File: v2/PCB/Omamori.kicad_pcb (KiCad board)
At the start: 2 copper layers, 25 x 35 mm, 27 parts, among them J1 Conn_01x04_Female, U1 BQ25504, U2 TPS61222DCK, U3 ATtiny85

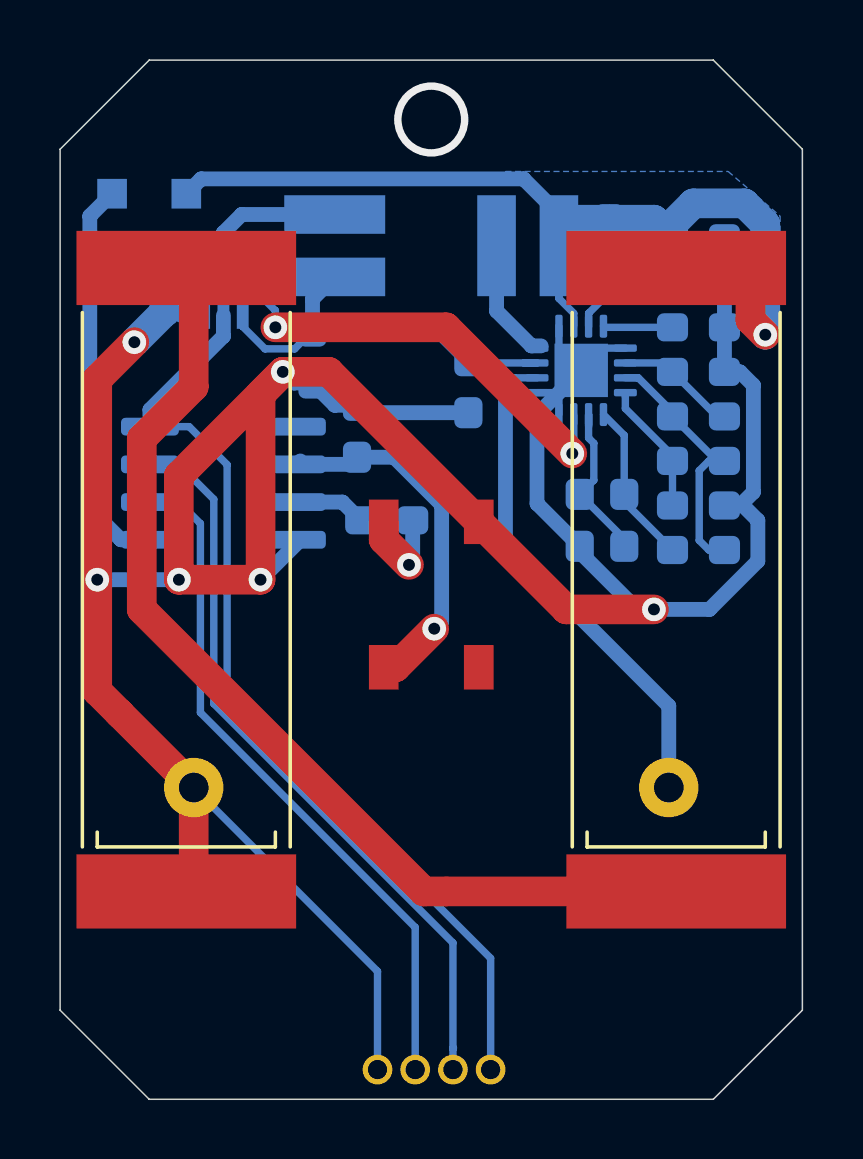
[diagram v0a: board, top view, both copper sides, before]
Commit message: Added reset button and changed a few wires.
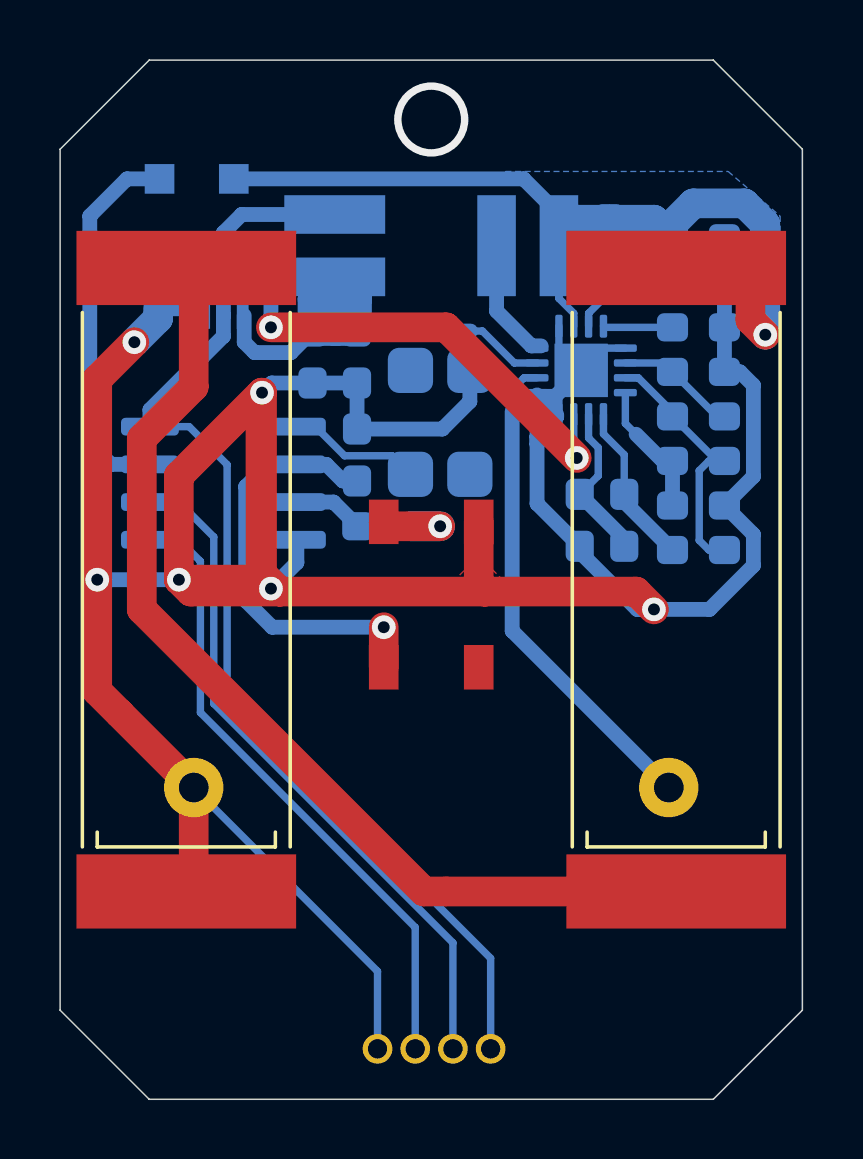
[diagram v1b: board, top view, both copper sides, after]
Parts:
- added U4: TS-1233, own_footprints:TS-1233, B.Cu at (25.3, 24.7)
- moved C_filter1 3.88 mm to (22.5, 22.5)
- moved D2 1.68 mm to (17.1, 16.5), turned to 180 degrees
- moved C_led1 0.80 mm to (22.5, 25.8)
- moved J1 0.70 mm to (27.0, 45.8)
- moved R_data1 0.22 mm to (23.4, 28.2)
- moved C_post_boost1 0.20 mm to (15.8, 20.0)
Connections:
- D1 pad 4: Net-(D1-Pad4) -> (no net)
- U3 pad 1: Net-(U3-Pad1) -> /Reset
- U3 pad 5: /Vsolar_measure -> /Tx
- U3 pad 6: /Tx -> /Rx
- U3 pad 7: /Rx -> /Vsolar_measure
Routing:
- net GND: track 115.7 -> 128.4 mm
- net /Vstor: track 14.0 -> 21.1 mm
- net /Reset: track 0.00 -> 4.49 mm
- net /Vcc_LED: track 13.1 -> 15.2 mm
- net /Rx: track 25.2 -> 23.2 mm
- net /Tx: track 23.4 -> 21.4 mm
- net /Vsolar: track 34.4 -> 32.5 mm
- net /Vcc_ATTiny: track 35.9 -> 34.9 mm
- net /Vsolar_measure: track 13.4 -> 12.8 mm

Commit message: Updated program and modified PCB Layout to measure V_supercap.
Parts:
- moved D2 15.3 mm to (15.3, 31.7), turned to 90 degrees
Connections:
- net /Vsolar_measure renamed /Vmeasure
- D2 pad 2: /Vsolar -> Net-(C_super1-Pad1)
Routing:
- net Net-(C_super1-Pad1): track 16.8 -> 31.8 mm, vias 0 -> 2
- net /Vsolar: track 32.5 -> 23.3 mm
- net /Vmeasure: track 12.8 -> 6.16 mm
- net GND: track 128.4 -> 129.8 mm
- net Net-(Sol_1-Pad2): track 33.9 -> 35.3 mm
- removed copper zone on B.Cu, net /Vsolar

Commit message: Final version + gerber export.
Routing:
- net GND: track 129.8 -> 128.7 mm
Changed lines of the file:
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@@
   )
   (setup
-    (last_trace_width 1)
+    (last_trace_width 0.25)
     (user_trace_width 0.5)
     (user_trace_width 1)
@@
     (add_net "Net-(C_ref1-Pad1)")
     (add_net "Net-(C_super1-Pad1)")
-    (add_net "Net-(D1-Pad4)")
     (add_net "Net-(L_boost1-Pad2)")
     (add_net "Net-(L_bst1-Pad2)")
@@
     (add_net "Net-(R_uv1-Pad2)")
     (add_net "Net-(Sol_1-Pad2)")
-    (add_net "Net-(U4-Pad1)")
-    (add_net "Net-(U4-Pad4)")
   )
   (module own_footprints:TS-1233 (layer B.Cu)
@@
     )
   )
+  (gr_line (start 15.5 12.5) (end 34.5 12.5) (layer Edge.Cuts) (width 0.05))
+  (gr_line (start 34.5 12.5) (end 37.5 15.5) (layer Edge.Cuts) (width 0.05))
+  (gr_line (start 12.5 15.5) (end 15.5 12.5) (layer Edge.Cuts) (width 0.05))
   (gr_line (start 12.5 44.5) (end 12.5 15.5) (layer Edge.Cuts) (width 0.05))
   (gr_line (start 15.5 47.5) (end 12.5 44.5) (layer Edge.Cuts) (width 0.05))
@@
   (gr_line (start 37.5 44.5) (end 34.5 47.5) (layer Edge.Cuts) (width 0.05))
   (gr_line (start 37.5 15.5) (end 37.5 44.5) (layer Edge.Cuts) (width 0.05))
-  (gr_line (start 34.5 12.5) (end 37.5 15.5) (layer Edge.Cuts) (width 0.05))
-  (gr_line (start 15.5 12.5) (end 34.5 12.5) (layer Edge.Cuts) (width 0.05))
-  (gr_line (start 12.5 15.5) (end 15.5 12.5) (layer Edge.Cuts) (width 0.05))
   (via (at 25 14.5) (size 2.5) (drill 2) (layers F.Cu B.Cu) (net 0))
   (via (at 16.5 30) (size 0.8) (drill 0.4) (layers F.Cu B.Cu) (net 1))
@@
   (segment (start 23.19 43.19) (end 17 37) (width 0.25) (layer B.Cu) (net 1))
   (segment (start 16.875 36.875) (end 17 37) (width 0.25) (layer B.Cu) (net 1))
-  (segment (start 32.5 31) (end 32.5 31) (width 0.25) (layer F.Cu) (net 1))
-  (via (at 32.5 31) (size 0.8) (drill 0.4) (layers F.Cu B.Cu) (net 1))
+  (via (at 31.9 30.4) (size 0.8) (drill 0.4) (layers F.Cu B.Cu) (net 1))
   (segment (start 30 29.065685) (end 30 28.875) (width 0.25) (layer B.Cu) (net 1))
-  (segment (start 31.934315 31) (end 30 29.065685) (width 0.5) (layer B.Cu) (net 1))
-  (segment (start 32.5 31) (end 31.934315 31) (width 0.5) (layer B.Cu) (net 1))
   (via (at 19.6 30.3) (size 0.8) (drill 0.4) (layers F.Cu B.Cu) (net 1))
   (segment (start 20.475 28.655) (end 20.475 28.775) (width 0.25) (layer B.Cu) (net 1))
@@
   (segment (start 19.625 23.375) (end 19.3 23.7) (width 0.5) (layer B.Cu) (net 1))
   (segment (start 21 23.375) (end 19.625 23.375) (width 0.5) (layer B.Cu) (net 1))
-  (segment (start 32.5 31) (end 31.89999 30.39999) (width 1) (layer F.Cu) (net 1))
   (segment (start 26.6 30.2) (end 26.79999 30.39999) (width 1) (layer F.Cu) (net 1))
   (segment (start 26.6 28.05) (end 26.6 30.2) (width 1) (layer F.Cu) (net 1))
@@
   (segment (start 29 24) (end 30.05 22.95) (width 0.5) (layer B.Cu) (net 1))
   (segment (start 28.5625 27.4375) (end 30 28.875) (width 0.5) (layer B.Cu) (net 1))
-  (segment (start 35.85001 28.47501) (end 34.875 27.5) (width 0.5) (layer B.Cu) (net 1))
-  (segment (start 35.85001 29.522278) (end 35.85001 28.47501) (width 0.5) (layer B.Cu) (net 1))
-  (segment (start 34.372288 31) (end 35.85001 29.522278) (width 0.5) (layer B.Cu) (net 1))
-  (segment (start 32.5 31) (end 34.372288 31) (width 0.5) (layer B.Cu) (net 1))
   (segment (start 34.875 27.497288) (end 34.875 27.5) (width 0.5) (layer B.Cu) (net 1))
   (segment (start 35.85001 26.522278) (end 34.875 27.497288) (width 0.5) (layer B.Cu) (net 1))
@@
   (segment (start 16.1 31.7) (end 13.75 31.7) (width 0.5) (layer B.Cu) (net 1))
   (segment (start 16.5 31.3) (end 16.1 31.7) (width 0.5) (layer B.Cu) (net 1))
+  (segment (start 35.85001 29.84999) (end 35.3 30.4) (width 0.5) (layer B.Cu) (net 1))
+  (segment (start 35.3 30.4) (end 31.9 30.4) (width 0.5) (layer B.Cu) (net 1))
+  (segment (start 35.85001 28.47501) (end 35.85001 29.84999) (width 0.5) (layer B.Cu) (net 1))
+  (segment (start 34.875 27.5) (end 35.85001 28.47501) (width 0.5) (layer B.Cu) (net 1))
+  (segment (start 31.525 30.4) (end 30 28.875) (width 0.5) (layer B.Cu) (net 1))
+  (segment (start 31.9 30.4) (end 31.525 30.4) (width 0.5) (layer B.Cu) (net 1))
   (segment (start 30.8375 21.5) (end 30.8 21.4625) (width 0.25) (layer B.Cu) (net 2))
   (segment (start 33.125 21.5) (end 30.8375 21.5) (width 0.25) (layer B.Cu) (net 2))
   (segment (start 18 18.314998) (end 18 18.9) (width 0.5) (layer B.Cu) (net 3))
-  (segment (start 18.614998 17.7) (end 18 18.314998) (width 0.5) (layer B.Cu) (net 3))
-  (segment (start 18.614998 17.7) (end 21.75 17.7) (width 0.5) (layer B.Cu) (net 3))
+  (segment (start 18 18.089998) (end 18 18.314998) (width 0.5) (layer B.Cu) (net 3))
+  (segment (start 18.389998 17.7) (end 18 18.089998) (width 0.5) (layer B.Cu) (net 3))
+  (segment (start 21.75 17.7) (end 18.389998 17.7) (width 0.5) (layer B.Cu) (net 3))
   (segment (start 27.2 20.95) (end 28.37499 22.12499) (width 0.5) (layer B.Cu) (net 4))
   (segment (start 27.2 18.75) (end 27.2 20.95) (width 0.5) (layer B.Cu) (net 4))
@@
   (segment (start 18.65 21.1) (end 18.65 20.975) (width 0.25) (layer B.Cu) (net 11))
   (segment (start 22.5 21.625) (end 26.325 21.625) (width 0.5) (layer B.Cu) (net 11))
-  (segment (start 26.723452 21.625) (end 26.325 21.625) (width 0.25) (layer B.Cu) (net 11))
-  (segment (start 27.798452 22.7) (end 26.723452 21.625) (width 0.25) (layer B.Cu) (net 11))
-  (segment (start 28.5625 22.7) (end 27.798452 22.7) (width 0.25) (layer B.Cu) (net 11))
   (segment (start 19.050001 22.350001) (end 18.70001 22.00001) (width 0.5) (layer B.Cu) (net 11))
   (segment (start 18.70001 22.00001) (end 18.70001 21.1) (width 0.5) (layer B.Cu) (net 11))
@@
   (segment (start 22.5 20.55) (end 21.75 19.8) (width 1) (layer B.Cu) (net 11))
   (segment (start 22.5 21.625) (end 22.5 20.55) (width 1) (layer B.Cu) (net 11))
+  (segment (start 27.9 22.7) (end 28.5625 22.7) (width 0.25) (layer B.Cu) (net 11))
+  (segment (start 26.825 21.625) (end 27.9 22.7) (width 0.25) (layer B.Cu) (net 11))
+  (segment (start 26.325 21.625) (end 26.825 21.625) (width 0.25) (layer B.Cu) (net 11))
   (via (at 36.25 21.75) (size 0.8) (drill 0.4) (layers F.Cu B.Cu) (net 12))
   (segment (start 29.3 20.526978) (end 29.3 18.75) (width 0.25) (layer B.Cu) (net 12))
@@
   (segment (start 17.29999 19.35) (end 17.07499 19.125) (width 0.5) (layer B.Cu) (net 13))
   (segment (start 17.29999 19.659992) (end 17.29999 19.35) (width 0.5) (layer B.Cu) (net 13))
+  (segment (start 17.07499 19.125) (end 17.29999 18.9) (width 0.5) (layer B.Cu) (net 13))
   (segment (start 33.125 36.875) (end 33 37) (width 0.25) (layer B.Cu) (net 14))
   (segment (start 28.126978 23.2) (end 28.5625 23.2) (width 0.25) (layer B.Cu) (net 14))
@@
   (segment (start 25.3 28.2) (end 23.55 28.2) (width 1) (layer F.Cu) (net 18))
   (segment (start 24.275 28.2) (end 25.3 28.2) (width 1) (layer B.Cu) (net 18))
-  (segment (start 14.55 26.115) (end 13.9 26.765) (width 0.5) (layer B.Cu) (net 23))
-  (segment (start 15.525 26.115) (end 14.55 26.115) (width 0.5) (layer B.Cu) (net 23))
-  (segment (start 13.9 29.05) (end 15.3 30.45) (width 0.5) (layer B.Cu) (net 23))
-  (segment (start 13.9 26.765) (end 13.9 29.05) (width 0.5) (layer B.Cu) (net 23))
   (segment (start 25.73 45.792894) (end 25.75 45.772894) (width 0.25) (layer B.Cu) (net 19))
   (segment (start 25.73 42.23) (end 17.675011 34.175011) (width 0.25) (layer B.Cu) (net 19))
@@
   (segment (start 23.67499 25.82499) (end 22.07948 25.82499) (width 0.25) (layer B.Cu) (net 22))
   (segment (start 24.3 26.45) (end 23.67499 25.82499) (width 0.25) (layer B.Cu) (net 22))
+  (segment (start 14.55 26.115) (end 13.9 26.765) (width 0.5) (layer B.Cu) (net 23))
+  (segment (start 15.525 26.115) (end 14.55 26.115) (width 0.5) (layer B.Cu) (net 23))
+  (segment (start 13.9 29.05) (end 15.3 30.45) (width 0.5) (layer B.Cu) (net 23))
+  (segment (start 13.9 26.765) (end 13.9 29.05) (width 0.5) (layer B.Cu) (net 23))
   (zone (net 1) (net_name GND) (layer F.Cu) (hatch edge 0.508)
     (connect_pads yes (clearance 0))

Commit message: Beyond last second changes to the PCB design and gerber files.
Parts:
- added R_oc1: 6.2M, Resistor_SMD:R_0603_1608Metric_Pad0.98x0.95mm_HandSolder, B.Cu at (31.0, 19.0)
- R_oc1_10: renamed from R_oc1; value 3.9M -> 10M
- R_oc2: value 6.2M -> 3.9M
- moved R_oc1_10 3.47 mm to (34.0, 17.0), turned to 180 degrees
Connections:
- R_oc1_10 pad 2: Net-(R_oc1-Pad2) -> Net-(R_oc1-Pad1)
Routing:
- net /Vsolar: track 23.3 -> 28.9 mm
- net Net-(R_oc1-Pad1): track 0.00 -> 2.57 mm

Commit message: Changes made to Roc1 and Roc2.
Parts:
- moved R_oc1_10 3.00 mm to (34.0, 20.0)
- moved R_oc2 3.00 mm to (34.0, 17.0), turned to 180 degrees
- moved R_oc1 0.50 mm to (31.5, 19.0), turned to 90 degrees
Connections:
- R_oc1_10 pad 1: /Vsolar -> GND
- R_oc2 pad 1: Net-(R_oc1-Pad2) -> /Vsolar
- R_oc2 pad 2: GND -> Net-(R_oc1-Pad2)
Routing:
- net Net-(R_oc1-Pad2): track 4.00 -> 5.95 mm
- net Net-(R_oc1-Pad1): track 2.57 -> 1.66 mm
- net /Vsolar: track 28.9 -> 28.0 mm
